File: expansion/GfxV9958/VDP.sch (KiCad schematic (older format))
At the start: 13 parts, among them U10 41464, U11 V9958, U5 41464, U6 41464, U7 41464, U8 41464, U9 41464, Y2 21.443Mhz

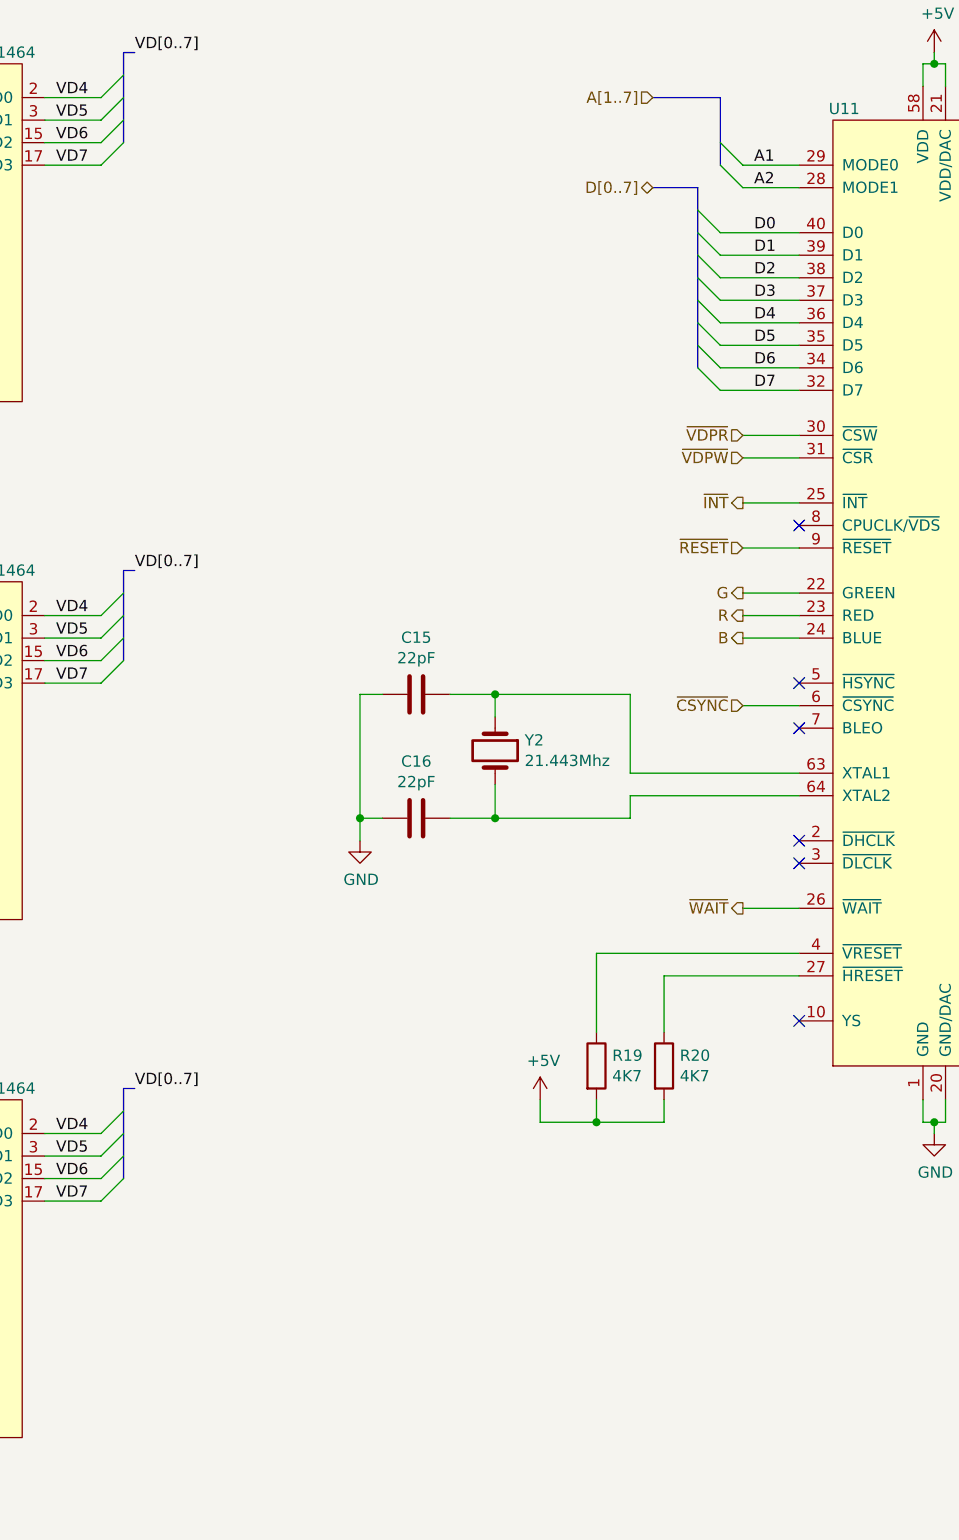
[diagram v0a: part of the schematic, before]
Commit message: Added Eth8019 and updated page description for all projects
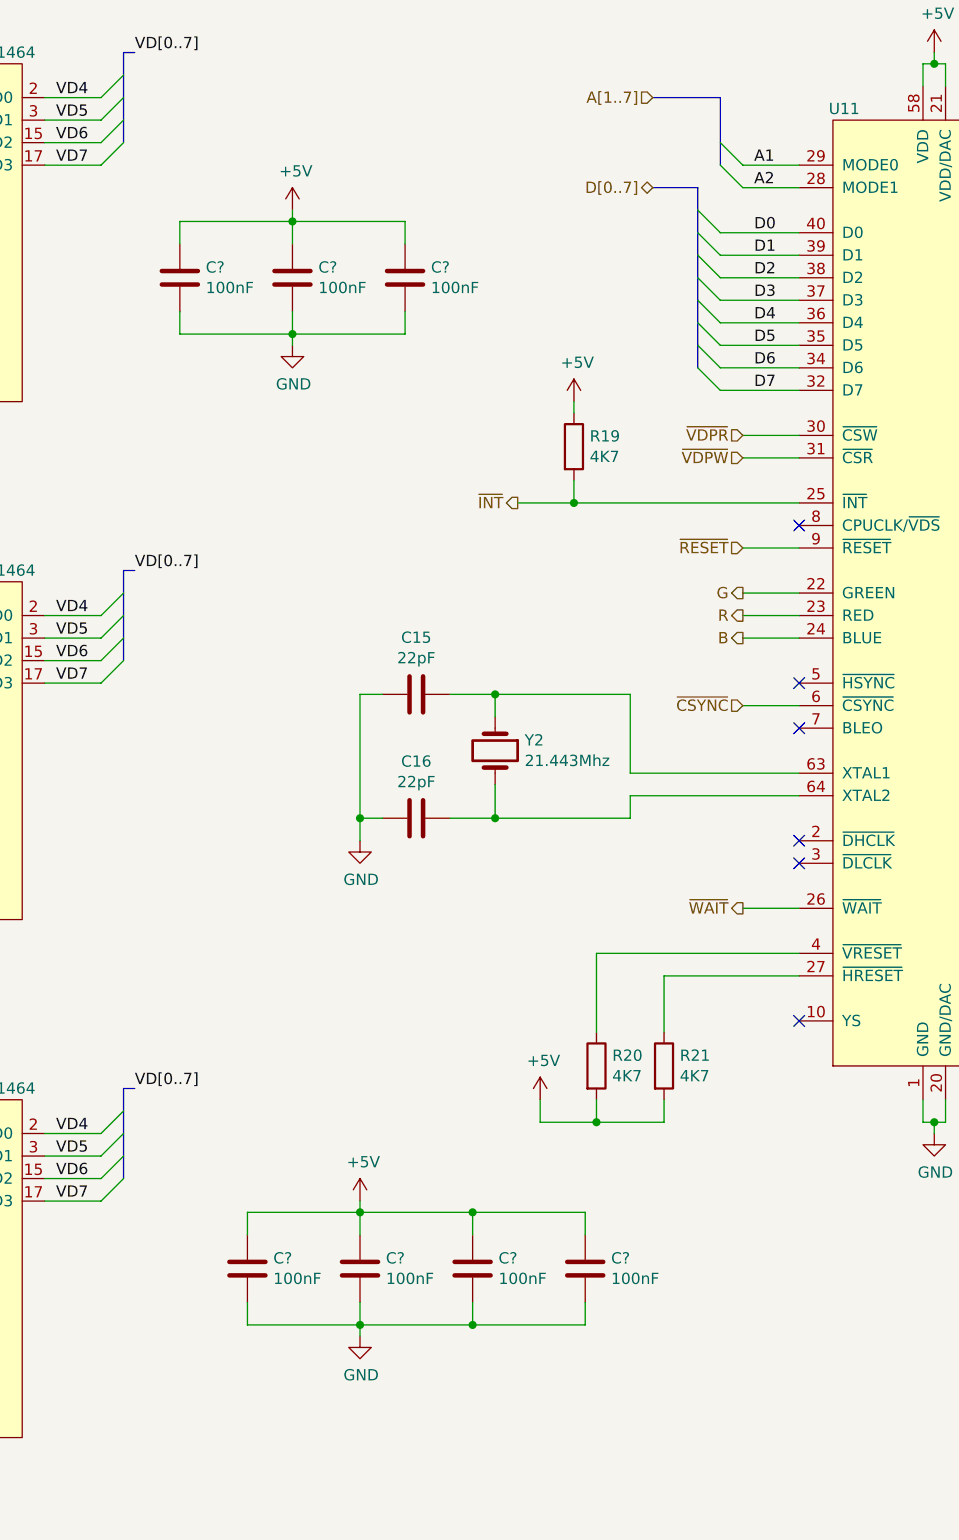
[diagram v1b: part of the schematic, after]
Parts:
- added C? (x7): 100nF, symbol Device:C
- added R19: 4K7, symbol Device:R
- renumbered R19 to R20, R20 to R21
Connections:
- net +5V: now also C?.1, C?.1, C?.1, C?.1, C?.1, C?.1, C?.1, R19.1
- net GND: now also C?.2, C?.2, C?.2, C?.2, C?.2, C?.2, C?.2
- net ~INT: now also R19.2

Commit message: Updated Mini Din footprints
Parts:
- C18, C19, C20, C21, C22, C25, C26: renamed from C?; footprint (none) -> Capacitor_THT:C_Disc_D5.0mm_W2.5mm_P2.50mm
- C23: renamed from C15; footprint (none) -> Capacitor_THT:C_Disc_D5.0mm_W2.5mm_P2.50mm
- C24: renamed from C16; footprint (none) -> Capacitor_THT:C_Disc_D5.0mm_W2.5mm_P2.50mm
- C27: renamed from C17; value C -> 100nF; footprint (none) -> Capacitor_THT:C_Disc_D5.0mm_W2.5mm_P2.50mm
- R19, R20, R21: footprint (none) -> Resistor_THT:R_Axial_DIN0207_L6.3mm_D2.5mm_P10.16mm_Horizontal
- U10, U5, U6, U7, U8, U9: footprint (none) -> Package_DIP:DIP-18_W7.62mm_Socket
- U11: footprint (none) -> Ddraig:DIP-64-V9958
- Y2: footprint (none) -> Crystal:Crystal_HC50_Vertical
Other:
- moved on the sheet: C18, C19, C20, C21, C22, C23, C24, C25, C26, C27, R19, R20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
